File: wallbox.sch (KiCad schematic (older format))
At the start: 40 parts, among them J1 From Transformer, J2 To Wallbox, J3 To Microcontroller, Q1 BC547, Q2 BC547, Q3 BC547, U1 KA78R33, U2 LM7805CT, U3 TPC817MC, U4 TPC817MC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

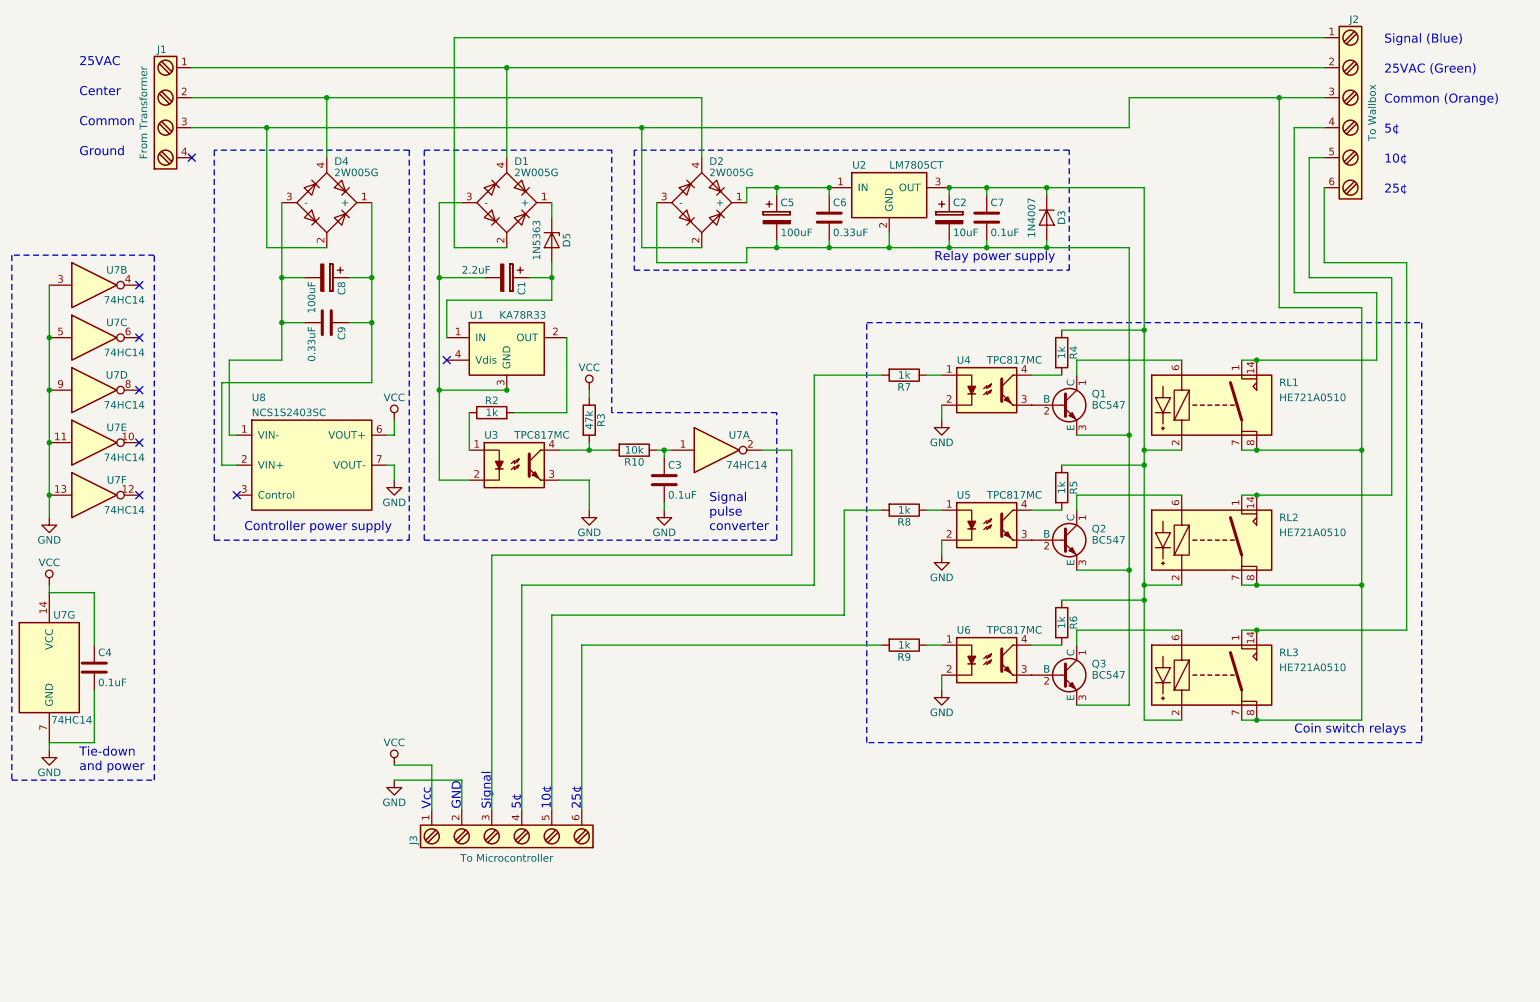
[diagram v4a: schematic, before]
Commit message: Added ESP8266 to the schematic
Hopefully the schematic is actually final now, or close to it.
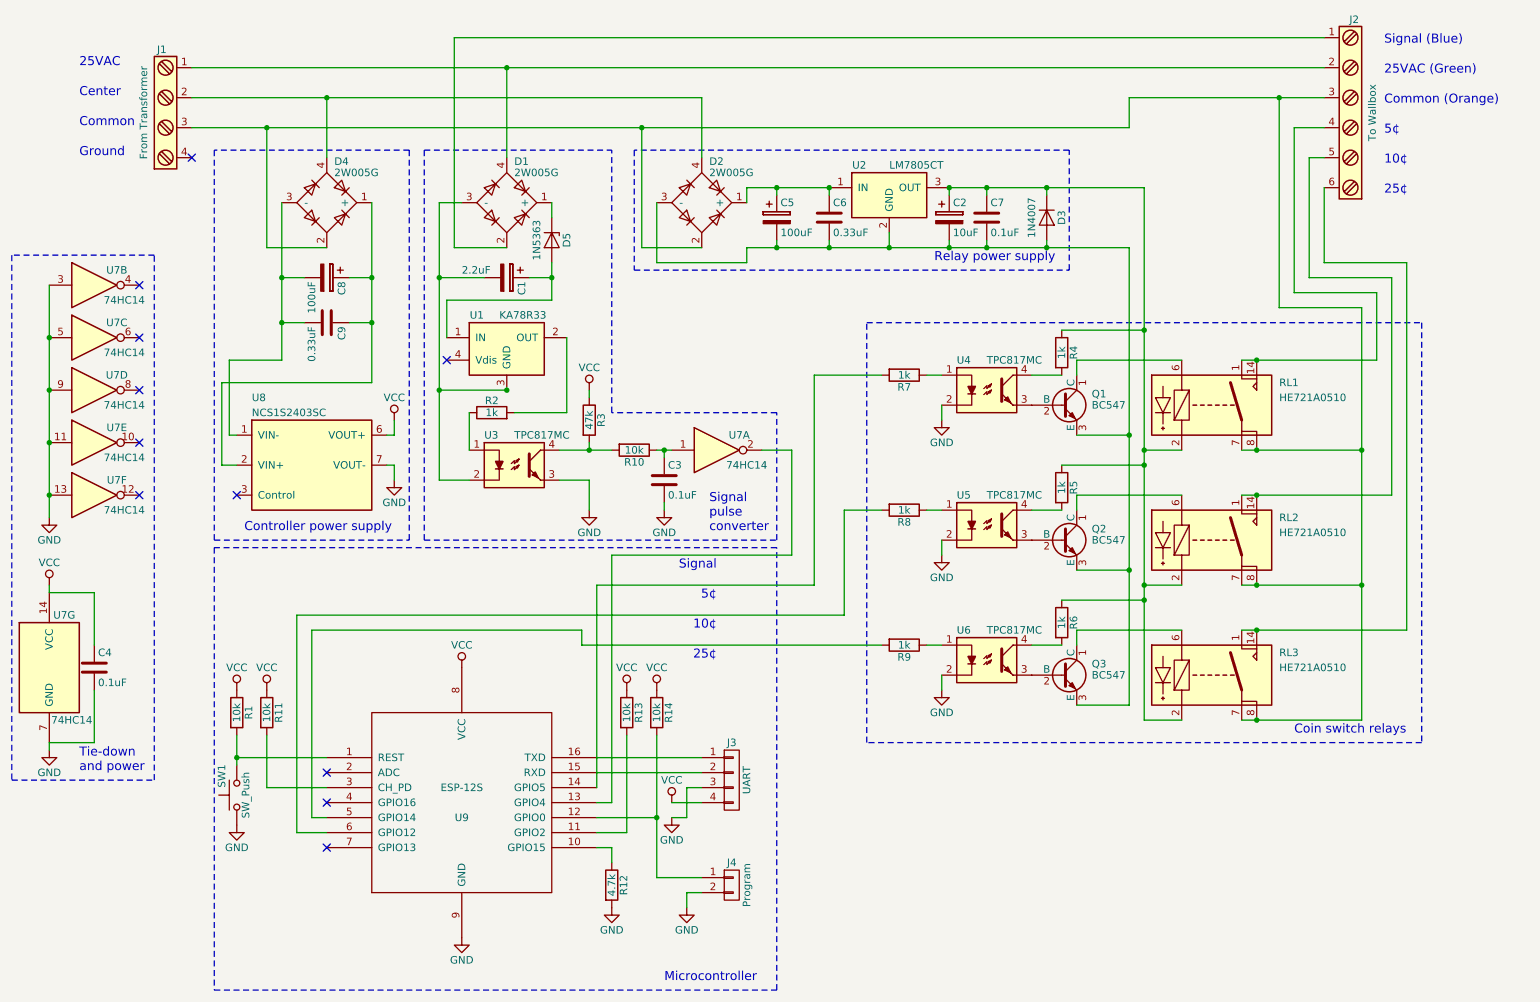
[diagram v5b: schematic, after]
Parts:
- removed J3: To Microcontroller, Connectors_Terminal_Blocks:TerminalBlock_Pheonix_MKDS1.5-6pol, symbol Screw_Terminal_1x06
- added J3: UART, Pin_Headers:Pin_Header_Straight_1x04_Pitch2.54mm, symbol CONN_01X04
- added J4: Program, Pin_Headers:Pin_Header_Straight_1x02_Pitch2.54mm, symbol CONN_01X02
- added R1, R11, R13, R14: 10k, Resistors_THT:R_Axial_DIN0207_L6.3mm_D2.5mm_P10.16mm_Horizontal, symbol R
- added R12: 4.7k, Resistors_THT:R_Axial_DIN0207_L6.3mm_D2.5mm_P10.16mm_Horizontal, symbol R
- added SW1: SW_Push, Buttons_Switches_THT:SW_PUSH_6mm_h5mm, symbol SW_Push
- added U9: ESP-12S, wallbox-footprints:ESP-12S_SMD, symbol ESP-12
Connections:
- net GND: now also J3.3 (P3), J4.2 (P2), R12.2, SW1.1, U9.9 (GND)
- net VCC: now also J3.4 (P4), R1.1, R11.1, R13.1, R14.1, U9.8 (VCC)
- net at U7.2: now also U9.13 (GPIO4)
- net at R7.2: now also U9.14 (GPIO5)
- net at R8.2: now also U9.6 (GPIO12)
- net at R9.2: now also U9.5 (GPIO14)
- new net: R1.2, SW1.2, U9.1 (REST)
- new net: R12.1, U9.10 (GPIO15)
- new net: R13.2, U9.11 (GPIO2)
- new net: J4.1 (P1), R14.2, U9.12 (GPIO0)
- new net: J3.2 (P2), U9.15 (RXD)
- new net: J3.1 (P1), U9.16 (TXD)
- new net: R11.2, U9.3 (CH_PD)
- no-connect marks 8 -> 11
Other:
- note added: "Microcontroller"
- note removed: "GND"
- note removed: "Vcc"

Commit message: More progress, added board outline
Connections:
- net at J2.1: now also RL3.1, RL3.14; no longer D1.2
- net at D1.4, J1.1 (25VAC): now also J2.5; no longer J2.2
- net at D2.2, D4.2, J1.3 (Common)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: now also J2.4; no longer J2.3
- net at RL1.1, RL1.14: now also J2.3; no longer J2.4
- net at RL2.1, RL2.14: now also J2.2; no longer J2.5
- new net: D1.2, J2.6
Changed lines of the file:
@@
 F 4 "CONN TERM BLOCK 6POS 5MM PCB" H 9450 1600 60  0001 C CNN "Description"
 	1    9450 1600
-	-1   0    0    -1
+	-1   0    0    1
 $EndComp
 Text Notes 950  1300 0    60   ~ 0

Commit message: First pass of post-rev-A fixes
Removed Zener diode, that's probably unnecessary and  wasn't working as
intended.
Fixed coin relay connections (25VAC instead of Common)
Tweaked some component labels/values
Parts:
- removed D5: 1N5363, Diodes_THT:D_DO-41_SOD81_P12.70mm_Horizontal, symbol D_Zener
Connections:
- net at RL1.7, RL1.8, RL2.7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: now also D1.4, J1.1 (25VAC), J2.5; no longer D2.2, D4.2, J1.3 (Common), J2.4
- net at D1.1 (+): now also C1.1, U1.1 (IN)
- new net: D2.2, D4.2, J1.3 (Common), J2.4
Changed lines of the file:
@@
 	1700 1700 7950 1700
 Wire Wire Line
-	4100 2600 4100 2850
+	4100 2200 4100 2850
 Wire Wire Line
 	4100 2850 3400 2850
@@
 	9250 2600 9800 2600
 Wire Wire Line
-	9800 2600 9800 5050
-Wire Wire Line
-	9800 5050 8700 5050
+	9800 5050 9800 2600
+Wire Wire Line
+	8700 5050 9800 5050
 Wire Wire Line
 	9250 1900 9150 1900
@@
 	9150 2700 9700 2700
 Wire Wire Line
-	9700 2700 9700 4150
-Wire Wire Line
-	9700 4150 8700 4150
+	9700 4150 9700 2700
+Wire Wire Line
+	8700 4150 9700 4150
 Wire Wire Line
 	9250 1700 9050 1700
@@
 	9050 2800 9600 2800
 Wire Wire Line
-	9600 2800 9600 3250
-Wire Wire Line
-	9600 3250 8700 3250
+	9600 3250 9600 2800
+Wire Wire Line
+	8700 3250 9600 3250
 Connection ~ 8800 3250
 Connection ~ 8800 4150
 Connection ~ 8800 5050
 Wire Wire Line
-	8950 1500 8950 2900
-Wire Wire Line
 	8950 2900 9500 2900
 Wire Wire Line
-	9500 2900 9500 5650
-Wire Wire Line
-	9500 5650 8700 5650
-Connection ~ 8950 1500
+	9500 5650 9500 2900
+Wire Wire Line
+	8700 5650 9500 5650
 Wire Wire Line
 	8700 4750 9500 4750
@@
 Controller power supply
 $Comp
-L D_Zener D5
-U 1 1 59DD44FB
-P 4100 2450
-F 0 "D5" H 4100 2550 50  0000 C CNN
-F 1 "1N5363" H 4100 2350 50  0000 C CNN
-F 2 "Diodes_THT:D_DO-41_SOD81_P12.70mm_Horizontal" H 4100 2450 50  0001 C CNN
-F 3 "http://www.onsemi.com/pub/Collateral/1N5333B-D.PDF" H 4100 2450 50  0001 C CNN
-F 4 "DIODE ZENER 30V 5W AXIAL" H 4100 2450 60  0001 C CNN "Description"
-	1    4100 2450
-	0    1    1    0
-$EndComp
-Wire Wire Line
-	4100 2300 4100 2200
-$Comp
 L ESP-12 U9
 U 1 1 59DEBB76
@@
 Text Notes 4850 7400 0    60   ~ 0
 Microcontroller
+Wire Wire Line
+	8950 2900 8950 1300
+Connection ~ 8950 1300
 $EndSCHEMATC
